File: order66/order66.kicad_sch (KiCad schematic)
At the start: 144 parts, among them J1 NICEVIEW, J2 Pouch Battery Connector, SW1 AUX1, SW10 A, SW11 Z, SW12 AUX7, SW13 RST, SW14 2, SW15 W, SW16 S, SW17 X, SW18 LALT, SW19 ON/OFF, SW2 ESC, SW20 3, SW21 E, SW22 D, SW23 C, SW24 GUI, SW25 AUX5, SW26 4, SW27 R, SW28 F, SW29 V, SW3 TAB, SW30 RAISE, SW31 AUX4, SW32 5, SW33 T, SW34 G, SW35 B, SW36 AUX3, SW37 AUX2, SW38 6, SW39 Y, SW4 CAPSLCK, SW40 H, SW41 N, SW42 RSPACE, SW44 7, SW45 U, SW46 J, SW47 M, SW48 LOWER, SW5 LSHIFT, SW50 8, SW51 I, SW52 K, SW53 ,<, SW54 LEFT, SW56 9, SW57 O, SW58 L, SW59 .>, SW6 LCTRL, SW60 DOWN, SW62 0, SW63 P, SW64 ;:, SW65 /?, SW66 UP, SW67 AUX6, SW68 BACKSPACE, SW69 BACKSLACH, SW7 LSPACE, SW70 ENTER, SW71 RSHIFT, SW72 RIGHT, SW8 1, SW9 Q, U1 NiceNano

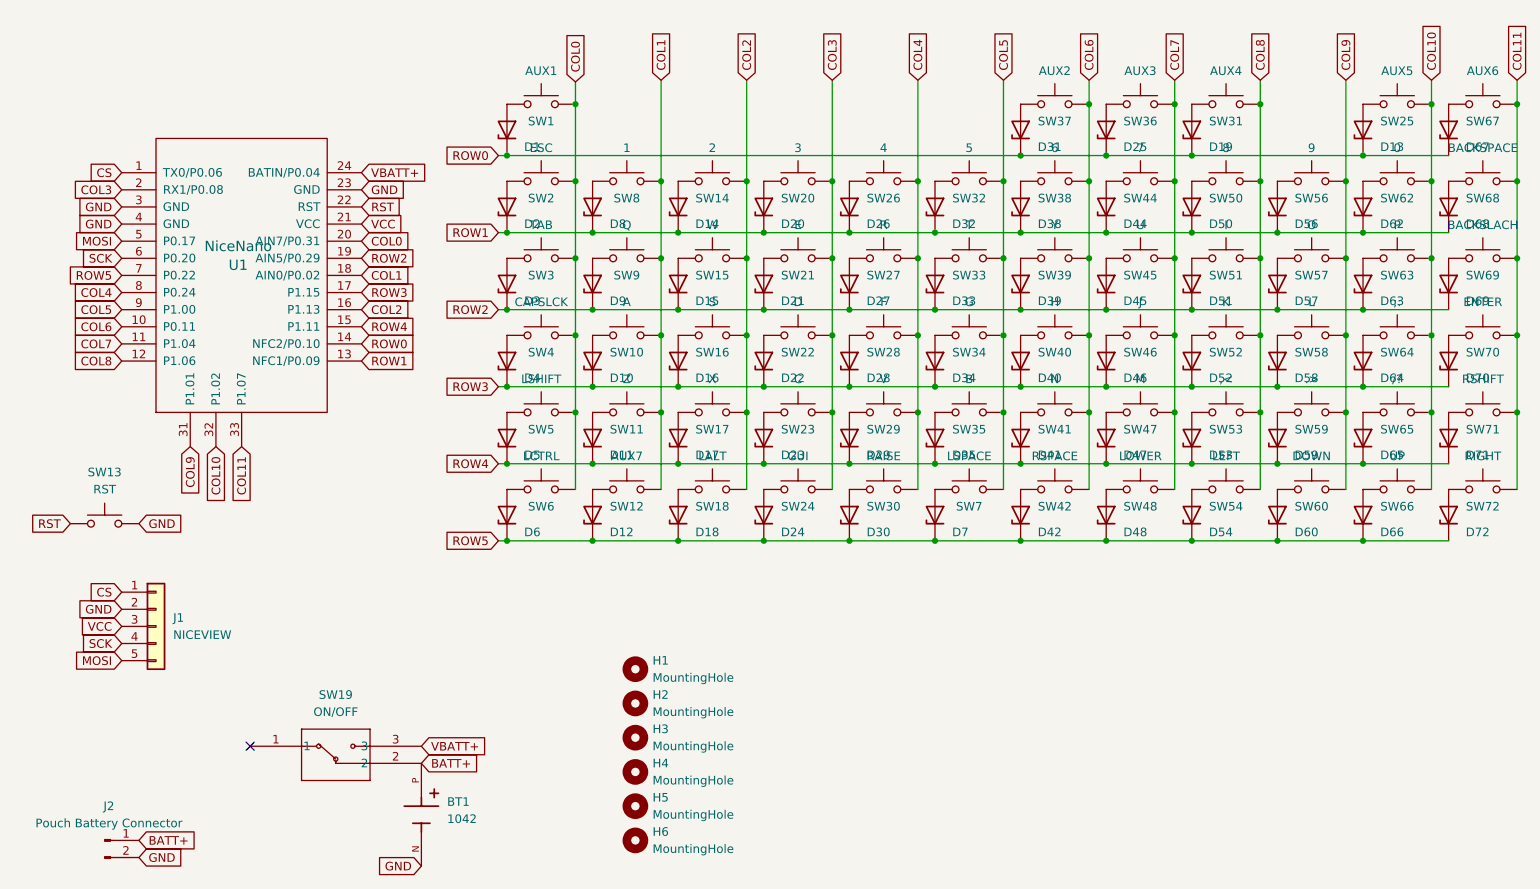
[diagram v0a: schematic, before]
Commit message: changed to through hole diodes in schematic
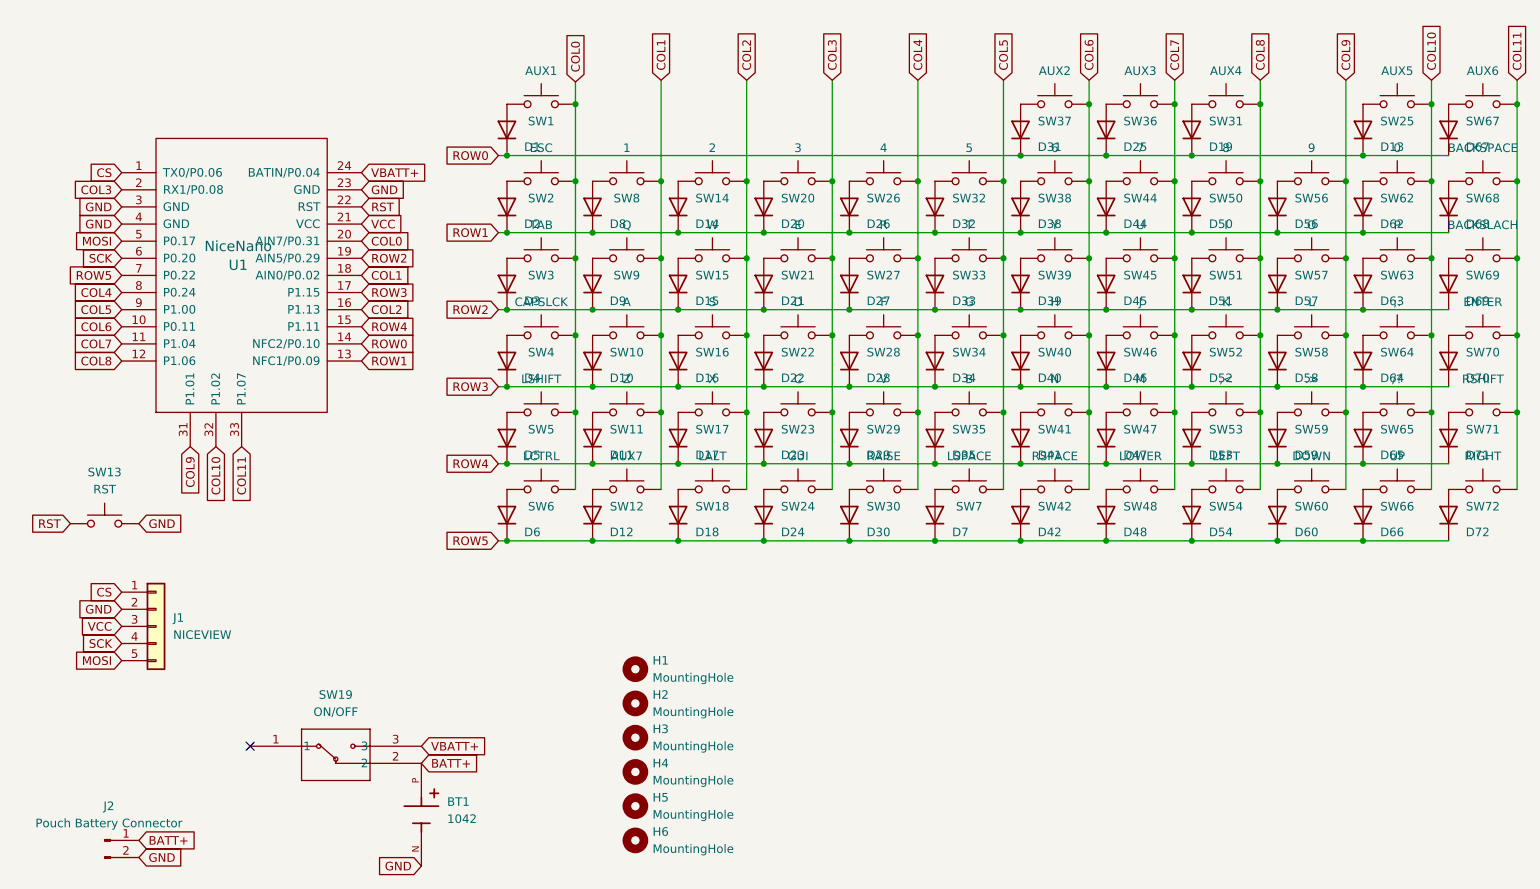
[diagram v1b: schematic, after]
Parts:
- D1, D10, D11, D12, D13, D14, D15, D16, D17, D18, D19, D2, D20, D21, D22, D23, D24, D25, D26, D27, D28, D29, D3, D30, D31, D32, D33, D34, D35, D38, D39, D4, D40, D41, D42, D44, D45, D46, D47, D48, D5, D50, D51, D52, D53, D54, D56, D57, D58, D59, D6, D60, D62, D63, D64, D65, D66, D67, D68, D69, D7, D70, D71, D72, D8, D9: footprint Diode_SMD:D_SOD-123 -> Diode_THT:D_DO-35_SOD27_P7.62mm_Horizontal; symbol Diode:1N47xxA -> Diode:1N4148

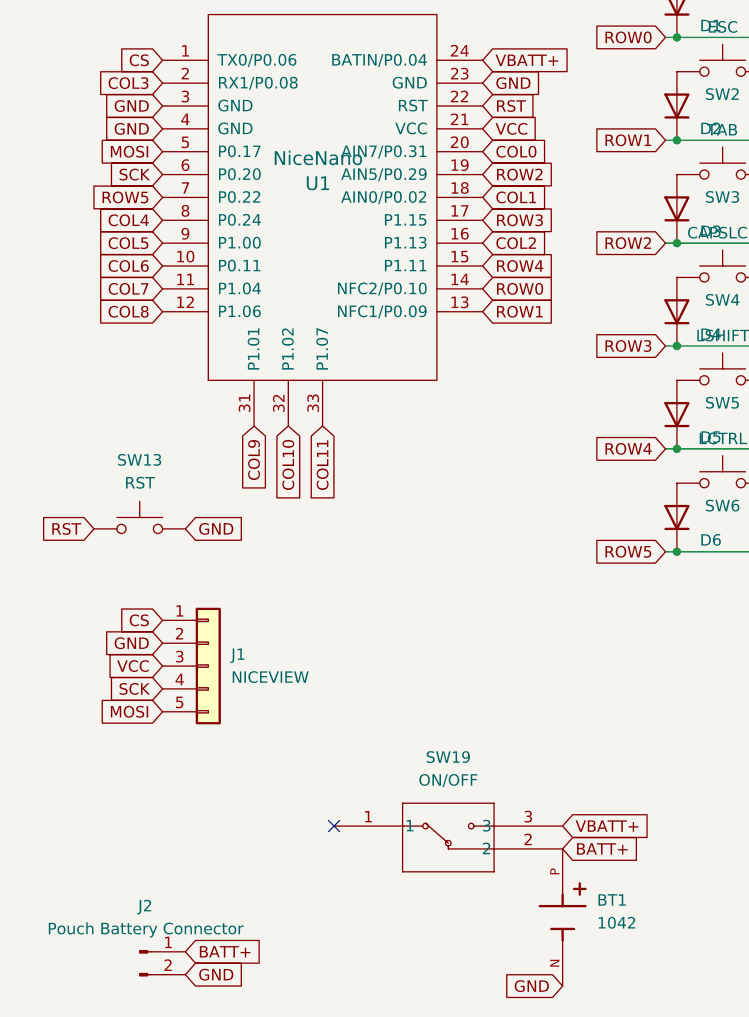
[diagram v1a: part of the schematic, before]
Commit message: moved to more through hole components and rerouted traces
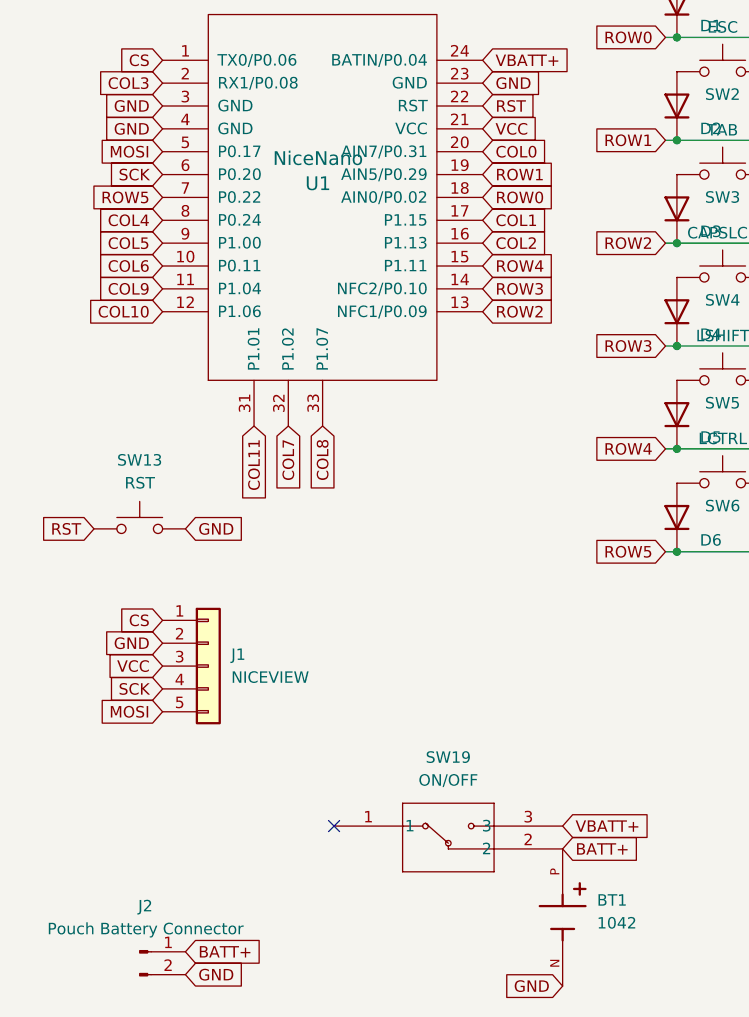
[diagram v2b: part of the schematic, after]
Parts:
- BT1: footprint 1042:BAT_1042 -> 1043P:BAT_1043P; symbol 1042:1042 -> 1043:1043P; PARTREV E -> D; SNAPEDA_PN 1042 -> 1043P
- D1, D10, D11, D12, D13, D14, D15, D16, D17, D18, D19, D2, D20, D21, D22, D23, D24, D25, D26, D27, D28, D29, D3, D30, D31, D32, D33, D34, D35, D38, D39, D4, D40, D41, D42, D44, D45, D46, D47, D48, D5, D50, D51, D52, D53, D54, D56, D57, D58, D59, D6, D60, D62, D63, D64, D65, D66, D67, D68, D69, D7, D70, D71, D72, D8, D9: value 1N47xxA -> 1N4148
- J2: footprint Connector_JST:JST_EH_S2B-EH_1x02_P2.50mm_Horizontal -> Connector_JST:JST_PH_B2B-PH-K_1x02_P2.00mm_Vertical
- SW13: footprint Button_Switch_SMD:SW_SPST_TL3342 -> Button_Switch_THT:SW_TH_Tactile_Omron_B3F-10xx
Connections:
- net COL1: now also U1.17 (P1.15); no longer U1.18 (AIN0/P0.02)
- net COL10: now also U1.12 (P1.06); no longer U1.32 (P1.02)
- net COL11: now also U1.31 (P1.01); no longer U1.33 (P1.07)
- net COL7: now also U1.32 (P1.02); no longer U1.11 (P1.04)
- net COL8: now also U1.33 (P1.07); no longer U1.12 (P1.06)
- net COL9: now also U1.11 (P1.04); no longer U1.31 (P1.01)
- net ROW0: now also U1.18 (AIN0/P0.02); no longer U1.14 (NFC2/P0.10)
- net ROW1: now also U1.19 (AIN5/P0.29); no longer U1.13 (NFC1/P0.09)
- net ROW2: now also U1.13 (NFC1/P0.09); no longer U1.19 (AIN5/P0.29)
- net ROW3: now also U1.14 (NFC2/P0.10); no longer U1.17 (P1.15)

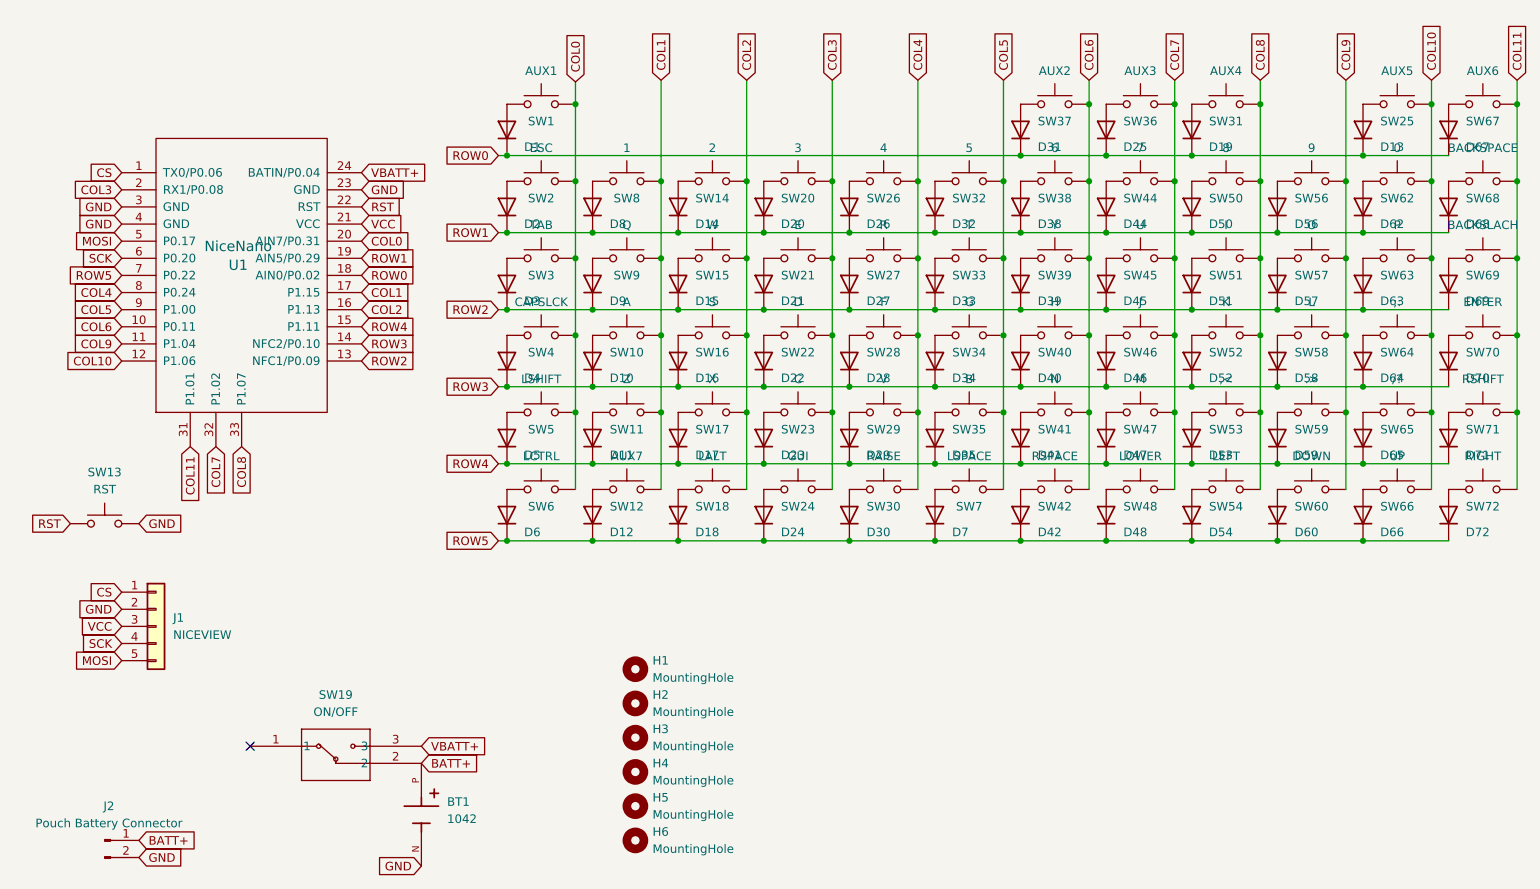
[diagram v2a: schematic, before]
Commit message: reordered the switch and diode numberings to be in order
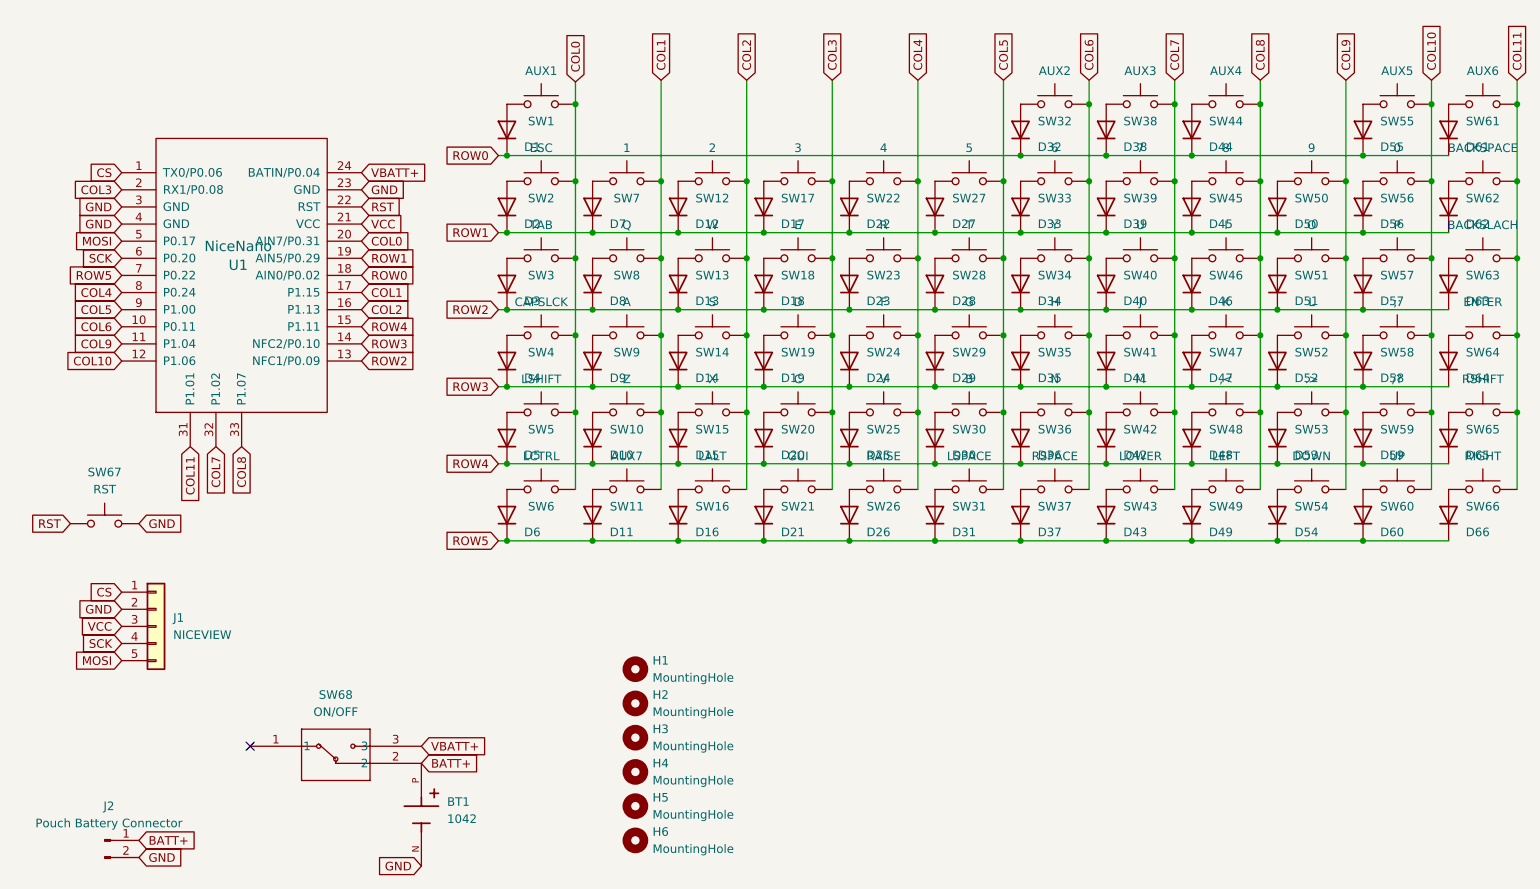
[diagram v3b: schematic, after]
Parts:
- renumbered D11 to D10, D12 to D11, D14 to D12, D15 to D13, D16 to D14, D17 to D15, D18 to D16, D20 to D17, D21 to D18, D22 to D19, D23 to D20, D24 to D21, D26 to D22, D27 to D23, D28 to D24, D29 to D25, D30 to D26, D32 to D27, D33 to D28, D34 to D29, D35 to D30, D7 to D31, D31 to D32, D38 to D33, D39 to D34, D40 to D35, D41 to D36, D42 to D37, D25 to D38, D44 to D39, D45 to D40, D46 to D41, D47 to D42, D48 to D43, D19 to D44, D50 to D45, D51 to D46, D52 to D47, D53 to D48, D54 to D49, D56 to D50, D57 to D51, D58 to D52, D59 to D53, D60 to D54, D13 to D55, D62 to D56, D63 to D57, D64 to D58, D65 to D59, D66 to D60, D67 to D61, D68 to D62, D69 to D63, D70 to D64, D71 to D65, D72 to D66, D8 to D7, D9 to D8, D10 to D9, SW11 to SW10, SW12 to SW11, SW14 to SW12, SW15 to SW13, SW16 to SW14, SW17 to SW15, SW18 to SW16, SW20 to SW17, SW21 to SW18, SW22 to SW19, SW23 to SW20, SW24 to SW21, SW26 to SW22, SW27 to SW23, SW28 to SW24, SW29 to SW25, SW30 to SW26, SW32 to SW27, SW33 to SW28, SW34 to SW29, SW35 to SW30, SW7 to SW31, SW37 to SW32, SW38 to SW33, SW39 to SW34, SW40 to SW35, SW41 to SW36, SW42 to SW37, SW36 to SW38, SW44 to SW39, SW45 to SW40, SW46 to SW41, SW47 to SW42, SW48 to SW43, SW31 to SW44, SW50 to SW45, SW51 to SW46, SW52 to SW47, SW53 to SW48, SW54 to SW49, SW56 to SW50, SW57 to SW51, SW58 to SW52, SW59 to SW53, SW60 to SW54, SW25 to SW55, SW62 to SW56, SW63 to SW57, SW64 to SW58, SW65 to SW59, SW66 to SW60, SW67 to SW61, SW68 to SW62, SW69 to SW63, SW70 to SW64, SW71 to SW65, SW72 to SW66, SW13 to SW67, SW19 to SW68, SW8 to SW7, SW9 to SW8, SW10 to SW9
